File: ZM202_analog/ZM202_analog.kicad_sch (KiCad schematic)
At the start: 1 part, among them J2 Conn_2x12_2.54_male

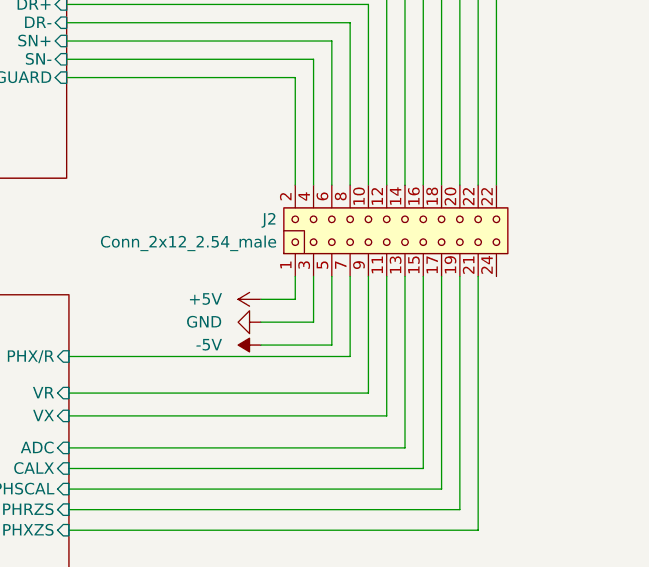
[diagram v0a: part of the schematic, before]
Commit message: Changed amplification resistor/cap in the analog core to 82nF/2.49k and did some various changes in the symbols and updated them into the schematic. Added PWR-flags
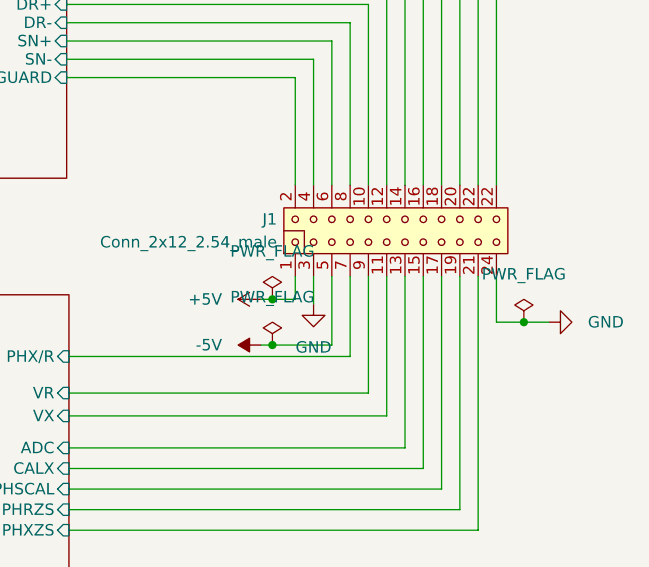
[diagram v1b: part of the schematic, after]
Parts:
- renumbered J2 to J1
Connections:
- net GND: now also J1.24
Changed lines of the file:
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@@
 (kicad_sch (version 20230121) (generator eeschema)
   (paper "A4")
-  (wire (pts (xy 171.958 87.884) (xy 175.768 87.884))
+  (junction (at 173.228 87.884) (diameter 0) (color 0 0 0 0)
+  )
+  (junction (at 173.228 92.964) (diameter 0) (color 0 0 0 0)
+  )
+  (junction (at 201.168 90.424) (diameter 0) (color 0 0 0 0)
+  )
+  (wire (pts (xy 171.958 87.884) (xy 173.228 87.884))
     (stroke (width 0) (type default))
   )
@@
     (stroke (width 0) (type default))
   )
-  (wire (pts (xy 171.958 90.424) (xy 177.8 90.424))
-    (stroke (width 0) (type default))
-  )
   (wire (pts (xy 150.622 111.252) (xy 194.056 111.252))
     (stroke (width 0) (type default))
   )
+  (wire (pts (xy 201.168 90.424) (xy 198.12 90.424))
+    (stroke (width 0) (type default))
+  )
   (wire (pts (xy 189.992 43.688) (xy 189.992 75.184))
     (stroke (width 0) (type default))
@@
     (stroke (width 0) (type default))
   )
-  (wire (pts (xy 171.958 92.964) (xy 179.832 92.964))
+  (wire (pts (xy 171.958 92.964) (xy 173.228 92.964))
     (stroke (width 0) (type default))
   )
@@
     (stroke (width 0) (type default))
   )
+  (wire (pts (xy 203.962 90.424) (xy 201.168 90.424))
+    (stroke (width 0) (type default))
+  )
   (wire (pts (xy 150.368 61.214) (xy 177.8 61.214))
     (stroke (width 0) (type default))
   )
+  (wire (pts (xy 173.228 92.964) (xy 179.832 92.964))
+    (stroke (width 0) (type default))
+  )
   (wire (pts (xy 196.088 35.814) (xy 196.088 75.184))
     (stroke (width 0) (type default))
@@
     (stroke (width 0) (type default))
   )
-  (wire (pts (xy 177.8 85.344) (xy 177.8 90.424))
+  (wire (pts (xy 177.8 85.344) (xy 177.8 88.392))
     (stroke (width 0) (type default))
   )
@@
     (stroke (width 0) (type default))
   )
+  (wire (pts (xy 173.228 87.884) (xy 175.768 87.884))
+    (stroke (width 0) (type default))
+  )
   (wire (pts (xy 150.368 57.15) (xy 181.864 57.15))
     (stroke (width 0) (type default))
@@
     (stroke (width 0) (type default))
   )
+  (wire (pts (xy 198.12 85.344) (xy 198.12 90.424))
+    (stroke (width 0) (type default))
+  )
   (wire (pts (xy 196.088 113.538) (xy 196.088 85.344))
     (stroke (width 0) (type default))
@@
   (symbol (lib_id "Jojos_Lib:Conn_2x12_2.54_male") (at 175.768 87.884 90) (unit 1)
     (in_bom yes) (on_board yes) (dnp no) (fields_autoplaced)
-    (property "Reference" "J2" (at 173.736 78.994 90)
+    (property "Reference" "J1" (at 173.736 78.994 90)
       (effects (font (size 1.27 1.27)) (justify left))
     )
@@
       (project "ZM202_analog"
         (path "/99a04650-e6a5-4da0-b985-3216476cb3cd"
-          (reference "J2") (unit 1)
+          (reference "J1") (unit 1)
         )
       )
@@
   (symbol (lib_id "power:-5V") (at 171.958 92.964 90) (unit 1)
     (in_bom yes) (on_board yes) (dnp no) (fields_autoplaced)
-    (property "Reference" "#PWR069" (at 169.418 92.964 0)
+    (property "Reference" "#PWR03" (at 169.418 92.964 0)
       (effects (font (size 1.27 1.27)) hide)
     )
@@
       (project "ZM202_analog"
         (path "/99a04650-e6a5-4da0-b985-3216476cb3cd"
-          (reference "#PWR069") (unit 1)
-        )
-      )
-    )
-  )
-  (symbol (lib_id "power:GND") (at 171.958 90.424 270) (unit 1)
-    (in_bom yes) (on_board yes) (dnp no) (fields_autoplaced)
-    (property "Reference" "#PWR067" (at 165.608 90.424 0)
-      (effects (font (size 1.27 1.27)) hide)
-    )
-    (property "Value" "GND" (at 167.64 90.424 90)
+          (reference "#PWR03") (unit 1)
+        )
+      )
+    )
+  )
+  (symbol (lib_id "power:GND") (at 177.8 88.392 0) (unit 1)
+    (in_bom yes) (on_board yes) (dnp no) (fields_autoplaced)
+    (property "Reference" "#PWR02" (at 177.8 94.742 0)
+      (effects (font (size 1.27 1.27)) hide)
+    )
+    (property "Value" "GND" (at 177.8 93.218 0)
+      (effects (font (size 1.27 1.27)))
+    )
+    (property "Footprint" "" (at 177.8 88.392 0)
+      (effects (font (size 1.27 1.27)) hide)
+    )
+    (property "Datasheet" "" (at 177.8 88.392 0)
+      (effects (font (size 1.27 1.27)) hide)
+    )
+    (pin "1")
+    (instances
+      (project "ZM202_analog"
+        (path "/99a04650-e6a5-4da0-b985-3216476cb3cd"
+          (reference "#PWR02") (unit 1)
+        )
+      )
+    )
+  )
+  (symbol (lib_id "power:GND") (at 203.962 90.424 90) (mirror x) (unit 1)
+    (in_bom yes) (on_board yes) (dnp no) (fields_autoplaced)
+    (property "Reference" "#PWR04" (at 210.312 90.424 0)
+      (effects (font (size 1.27 1.27)) hide)
+    )
+    (property "Value" "GND" (at 208.28 90.424 90)
       (effects (font (size 1.27 1.27)) (justify right))
     )
-    (property "Footprint" "" (at 171.958 90.424 0)
-      (effects (font (size 1.27 1.27)) hide)
-    )
-    (property "Datasheet" "" (at 171.958 90.424 0)
-      (effects (font (size 1.27 1.27)) hide)
-    )
-    (pin "1")
-    (instances
-      (project "ZM202_analog"
-        (path "/99a04650-e6a5-4da0-b985-3216476cb3cd"
-          (reference "#PWR067") (unit 1)
+    (property "Footprint" "" (at 203.962 90.424 0)
+      (effects (font (size 1.27 1.27)) hide)
+    )
+    (property "Datasheet" "" (at 203.962 90.424 0)
+      (effects (font (size 1.27 1.27)) hide)
+    )
+    (pin "1")
+    (instances
+      (project "ZM202_analog"
+        (path "/99a04650-e6a5-4da0-b985-3216476cb3cd"
+          (reference "#PWR04") (unit 1)
+        )
+      )
+    )
+  )
+  (symbol (lib_id "power:PWR_FLAG") (at 201.168 90.424 0) (unit 1)
+    (in_bom yes) (on_board yes) (dnp no) (fields_autoplaced)
+    (property "Reference" "#FLG01" (at 201.168 88.519 0)
+      (effects (font (size 1.27 1.27)) hide)
+    )
+    (property "Value" "PWR_FLAG" (at 201.168 85.09 0)
+      (effects (font (size 1.27 1.27)))
+    )
+    (property "Footprint" "" (at 201.168 90.424 0)
+      (effects (font (size 1.27 1.27)) hide)
+    )
+    (property "Datasheet" "~" (at 201.168 90.424 0)
+      (effects (font (size 1.27 1.27)) hide)
+    )
+    (pin "1")
+    (instances
+      (project "ZM202_analog"
+        (path "/99a04650-e6a5-4da0-b985-3216476cb3cd"
+          (reference "#FLG01") (unit 1)
         )
       )
@@
   (symbol (lib_id "power:+5V") (at 171.958 87.884 90) (unit 1)
     (in_bom yes) (on_board yes) (dnp no) (fields_autoplaced)
-    (property "Reference" "#PWR068" (at 175.768 87.884 0)
+    (property "Reference" "#PWR01" (at 175.768 87.884 0)
       (effects (font (size 1.27 1.27)) hide)
     )
@@
       (project "ZM202_analog"
         (path "/99a04650-e6a5-4da0-b985-3216476cb3cd"
-          (reference "#PWR068") (unit 1)
-        )
-      )
+          (reference "#PWR01") (unit 1)
+        )
+      )
+    )
+  )
+  (symbol (lib_id "power:PWR_FLAG") (at 173.228 87.884 0) (unit 1)
+    (in_bom yes) (on_board yes) (dnp no) (fields_autoplaced)
+    (property "Reference" "#FLG02" (at 173.228 85.979 0)
+      (effects (font (size 1.27 1.27)) hide)
+    )
+    (property "Value" "PWR_FLAG" (at 173.228 82.55 0)
+      (effects (font (size 1.27 1.27)))
+    )
+    (property "Footprint" "" (at 173.228 87.884 0)
+      (effects (font (size 1.27 1.27)) hide)
+    )
+    (property "Datasheet" "~" (at 173.228 87.884 0)
+      (effects (font (size 1.27 1.27)) hide)
+    )
+    (pin "1")
+    (instances
+      (project "ZM202_analog"
+        (path "/99a04650-e6a5-4da0-b985-3216476cb3cd"
+          (reference "#FLG02") (unit 1)
+        )
+      )
+    )
+  )
+  (symbol (lib_id "power:PWR_FLAG") (at 173.228 92.964 0) (unit 1)
+    (in_bom yes) (on_board yes) (dnp no) (fields_autoplaced)
+    (property "Reference" "#FLG03" (at 173.228 91.059 0)
+      (effects (font (size 1.27 1.27)) hide)
+    )
+    (property "Value" "PWR_FLAG" (at 173.228 87.63 0)
+      (effects (font (size 1.27 1.27)))
+    )
+    (property "Footprint" "" (at 173.228 92.964 0)
+      (effects (font (size 1.27 1.27)) hide)
+    )
+    (property "Datasheet" "~" (at 173.228 92.964 0)
+      (effects (font (size 1.27 1.27)) hide)
+    )
+    (pin "1")
+    (instances
+      (project "ZM202_analog"
+        (path "/99a04650-e6a5-4da0-b985-3216476cb3cd"
+          (reference "#FLG03") (unit 1)
+        )
+      )

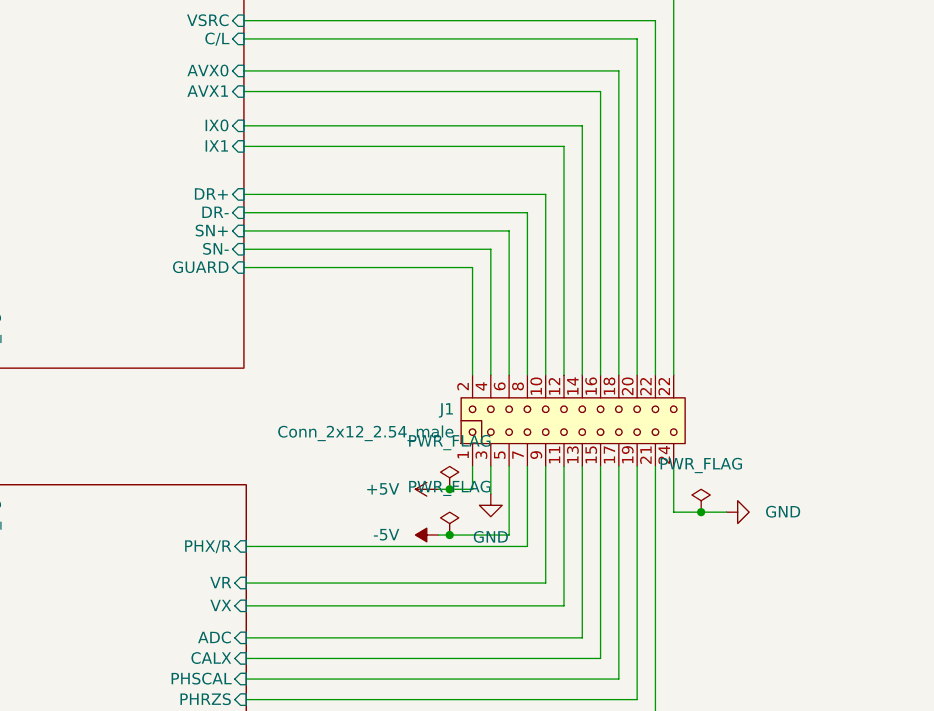
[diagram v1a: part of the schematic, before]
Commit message: Added 4-Pin connector for DUT
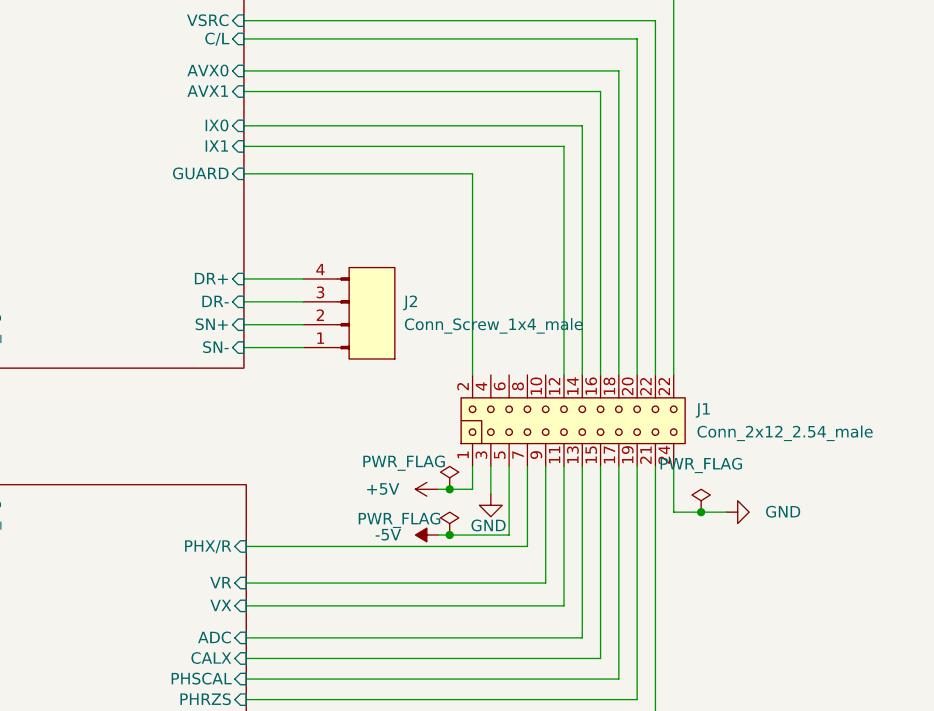
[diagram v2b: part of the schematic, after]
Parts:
- added J2: Conn_Screw_1x4_male, Connector_Phoenix_MC_HighVoltage:PhoenixContact_MCV_1,5_4-G-5.08_1x04_P5.08mm_Vertical, symbol Jojos_Lib:Conn_Screw_1x4_5.08mm
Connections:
- net AnalogCore/DR+: now also J2.4; no longer J1.10
- net AnalogCore/DR-: now also J2.3; no longer J1.8
- net AnalogCore/SN+: now also J2.2; no longer J1.6
- net AnalogCore/SN-: now also J2.1; no longer J1.4
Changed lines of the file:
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@@
-    (stroke (width 0) (type default))
-  )
-  (wire (pts (xy 183.896 55.118) (xy 183.896 75.184))
     (stroke (width 0) (type default))
   )
@@
     (stroke (width 0) (type default))
   )
-  (wire (pts (xy 150.368 59.182) (xy 179.832 59.182))
+  (wire (pts (xy 150.368 69.596) (xy 156.972 69.596))
     (stroke (width 0) (type default))
   )
@@
     (stroke (width 0) (type default))
   )
+  (wire (pts (xy 150.368 67.056) (xy 156.972 67.056))
+    (stroke (width 0) (type default))
+  )
   (wire (pts (xy 192.024 85.344) (xy 192.024 108.966))
     (stroke (width 0) (type default))
@@
     (stroke (width 0) (type default))
   )
+  (wire (pts (xy 150.368 72.136) (xy 156.972 72.136))
+    (stroke (width 0) (type default))
+  )
   (wire (pts (xy 84.074 36.576) (xy 80.01 36.576))
     (stroke (width 0) (type default))
@@
     (stroke (width 0) (type default))
   )
-  (wire (pts (xy 150.368 61.214) (xy 177.8 61.214))
-    (stroke (width 0) (type default))
-  )
   (wire (pts (xy 173.228 92.964) (xy 179.832 92.964))
     (stroke (width 0) (type default))
@@
     (stroke (width 0) (type default))
   )
-  (wire (pts (xy 175.768 63.246) (xy 175.768 75.184))
+  (wire (pts (xy 175.768 52.832) (xy 175.768 75.184))
     (stroke (width 0) (type default))
   )
@@
     (stroke (width 0) (type default))
   )
-  (wire (pts (xy 181.864 57.15) (xy 181.864 75.184))
-    (stroke (width 0) (type default))
-  )
   (wire (pts (xy 192.024 41.402) (xy 192.024 75.184))
     (stroke (width 0) (type default))
@@
     (stroke (width 0) (type default))
   )
-  (wire (pts (xy 150.368 57.15) (xy 181.864 57.15))
-    (stroke (width 0) (type default))
-  )
   (wire (pts (xy 114.808 74.422) (xy 114.808 87.376))
     (stroke (width 0) (type default))
@@
     (stroke (width 0) (type default))
   )
-  (wire (pts (xy 150.368 63.246) (xy 175.768 63.246))
+  (wire (pts (xy 150.368 52.832) (xy 175.768 52.832))
     (stroke (width 0) (type default))
   )
@@
     (stroke (width 0) (type default))
   )
-  (wire (pts (xy 150.368 55.118) (xy 183.896 55.118))
-    (stroke (width 0) (type default))
-  )
   (wire (pts (xy 150.622 106.68) (xy 189.992 106.68))
     (stroke (width 0) (type default))
@@
     (stroke (width 0) (type default))
   )
-  (wire (pts (xy 177.8 61.214) (xy 177.8 75.184))
-    (stroke (width 0) (type default))
-  )
   (wire (pts (xy 150.368 49.784) (xy 185.928 49.784))
     (stroke (width 0) (type default))
   )
-  (wire (pts (xy 179.832 59.182) (xy 179.832 75.184))
-    (stroke (width 0) (type default))
-  )
   (wire (pts (xy 150.368 47.498) (xy 187.96 47.498))
     (stroke (width 0) (type default))
   )
   (wire (pts (xy 150.368 43.688) (xy 189.992 43.688))
+    (stroke (width 0) (type default))
+  )
+  (wire (pts (xy 150.368 64.516) (xy 156.972 64.516))
     (stroke (width 0) (type default))
   )
   (symbol (lib_id "Jojos_Lib:Conn_2x12_2.54_male") (at 175.768 87.884 90) (unit 1)
     (in_bom yes) (on_board yes) (dnp no) (fields_autoplaced)
-    (property "Reference" "J1" (at 173.736 78.994 90)
-      (effects (font (size 1.27 1.27)) (justify left))
-    )
-    (property "Value" "Conn_2x12_2.54_male" (at 173.736 81.534 90)
-      (effects (font (size 1.27 1.27)) (justify left))
+    (property "Reference" "J1" (at 200.66 78.994 90)
+      (effects (font (size 1.27 1.27)) (justify right))
+    )
+    (property "Value" "Conn_2x12_2.54_male" (at 200.66 81.534 90)
+      (effects (font (size 1.27 1.27)) (justify right))
     )
     (property "Footprint" "Connector_PinHeader_2.54mm:PinHeader_2x12_P2.54mm_Vertical" (at 173.228 71.374 0)
@@
     )
   )
+  (symbol (lib_id "Jojos_Lib:Conn_Screw_1x4_5.08mm") (at 162.052 68.326 180) (unit 1)
+    (in_bom yes) (on_board yes) (dnp no) (fields_autoplaced)
+    (property "Reference" "J2" (at 168.148 67.056 0)
+      (effects (font (size 1.27 1.27)) (justify right))
+    )
+    (property "Value" "Conn_Screw_1x4_male" (at 168.148 69.596 0)
+      (effects (font (size 1.27 1.27)) (justify right))
+    )
+    (property "Footprint" "Connector_Phoenix_MC_HighVoltage:PhoenixContact_MCV_1,5_4-G-5.08_1x04_P5.08mm_Vertical" (at 145.542 70.866 0)
+      (effects (font (size 1.27 1.27)) (justify left) hide)
+    )
+    (property "Datasheet" "" (at 145.542 68.326 0)
+      (effects (font (size 1.27 1.27)) (justify left) hide)
+    )
+    (property "Description" "" (at 145.542 65.786 0)
+      (effects (font (size 1.27 1.27)) (justify left) hide)
+    )
+    (property "Height" "15.01" (at 145.542 63.246 0)
+      (effects (font (size 1.27 1.27)) (justify left) hide)
+    )
+    (property "Mouser Part Number" "571-2828363 " (at 145.542 60.706 0)
+      (effects (font (size 1.27 1.27)) (justify left) hide)
+    )
+    (property "Mouser Price/Stock" "" (at 145.542 58.166 0)
+      (effects (font (size 1.27 1.27)) (justify left) hide)
+    )
+    (property "Manufacturer_Name" "" (at 145.542 55.626 0)
+      (effects (font (size 1.27 1.27)) (justify left) hide)
+    )
+    (property "Manufacturer_Part_Number" "" (at 145.542 53.086 0)
+      (effects (font (size 1.27 1.27)) (justify left) hide)
+    )
+    (pin "1")
+    (pin "2")
+    (pin "3")
+    (pin "4")
+    (instances
+      (project "ZM202_analog"
+        (path "/99a04650-e6a5-4da0-b985-3216476cb3cd"
+          (reference "J2") (unit 1)
+        )
+      )
+    )
+  )
   (symbol (lib_id "power:-5V") (at 171.958 92.964 90) (unit 1)
-    (in_bom yes) (on_board yes) (dnp no) (fields_autoplaced)
+    (in_bom yes) (on_board yes) (dnp no)
     (property "Reference" "#PWR03" (at 169.418 92.964 0)
       (effects (font (size 1.27 1.27)) hide)
     )
-    (property "Value" "-5V" (at 167.64 92.964 90)
-      (effects (font (size 1.27 1.27)) (justify left))
+    (property "Value" "-5V" (at 166.37 92.964 90)
+      (effects (font (size 1.27 1.27)))
     )
     (property "Footprint" "" (at 171.958 92.964 0)
@@
   )
   (symbol (lib_id "power:GND") (at 177.8 88.392 0) (unit 1)
-    (in_bom yes) (on_board yes) (dnp no) (fields_autoplaced)
+    (in_bom yes) (on_board yes) (dnp no)
     (property "Reference" "#PWR02" (at 177.8 94.742 0)
       (effects (font (size 1.27 1.27)) hide)
     )
-    (property "Value" "GND" (at 177.8 93.218 0)
+    (property "Value" "GND" (at 177.546 91.948 0)
       (effects (font (size 1.27 1.27)))
     )
@@
   )
   (symbol (lib_id "power:PWR_FLAG") (at 173.228 87.884 0) (unit 1)
-    (in_bom yes) (on_board yes) (dnp no) (fields_autoplaced)
+    (in_bom yes) (on_board yes) (dnp no)
     (property "Reference" "#FLG02" (at 173.228 85.979 0)
       (effects (font (size 1.27 1.27)) hide)
     )
-    (property "Value" "PWR_FLAG" (at 173.228 82.55 0)
+    (property "Value" "PWR_FLAG" (at 168.148 84.836 0)
       (effects (font (size 1.27 1.27)))
     )
@@
   )
   (symbol (lib_id "power:PWR_FLAG") (at 173.228 92.964 0) (unit 1)
-    (in_bom yes) (on_board yes) (dnp no) (fields_autoplaced)
+    (in_bom yes) (on_board yes) (dnp no)
     (property "Reference" "#FLG03" (at 173.228 91.059 0)
       (effects (font (size 1.27 1.27)) hide)
     )
-    (property "Value" "PWR_FLAG" (at 173.228 87.63 0)
+    (property "Value" "PWR_FLAG" (at 167.64 91.186 0)
       (effects (font (size 1.27 1.27)))
     )
@@
       (effects (font (size 1.27 1.27)) (justify left))
     )
-    (pin "DR+" input (at 150.368 55.118 0)
+    (pin "DR+" input (at 150.368 64.516 0)
       (effects (font (size 1.27 1.27)) (justify right))
     )
@@
       (effects (font (size 1.27 1.27)) (justify right))
     )
-    (pin "SN-" input (at 150.368 61.214 0)
-      (effects (font (size 1.27 1.27)) (justify right))
-    )
-    (pin "SN+" input (at 150.368 59.182 0)
-      (effects (font (size 1.27 1.27)) (justify right))
-    )
-    (pin "DR-" input (at 150.368 57.15 0)
+    (pin "SN-" input (at 150.368 72.136 0)
+      (effects (font (size 1.27 1.27)) (justify right))
+    )
+    (pin "SN+" input (at 150.368 69.596 0)
+      (effects (font (size 1.27 1.27)) (justify right))
+    )
+    (pin "DR-" input (at 150.368 67.056 0)
       (effects (font (size 1.27 1.27)) (justify right))
     )
@@
       (effects (font (size 1.27 1.27)) (justify right))
     )
-    (pin "GUARD" input (at 150.368 63.246 0)
-      (effects (font (size 1.27 1.27)) (justify right))
-    )
+    (pin "GUARD" input (at 150.368 52.832 0)
+      (effects (font (size 1.27 1.27)) (justify right))
+    )
